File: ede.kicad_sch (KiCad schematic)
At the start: 111 parts, among them J1 Conn_01x01, J10 Conn_01x01, J11 Conn_01x01, J12 Conn_01x01, J2 Conn_01x01, J3 Conn_01x01, J4 Conn_01x01, J5 Conn_01x06, J6 Conn_01x01, J7 Conn_01x04, J8 Conn_01x04, J9 Conn_01x01, Q1 MDP10N027, Q2 MDP10N027, Q3 MDP10N027, Q4 MDP10N027, Q5 MDP10N027, Q6 MDP10N027, U1 Blackpill, U2 NCS20034DR2G, U3 STH0548S12, U4 MP1584EN_4pin, U5 U3216, U6 U3216, U7 U3216

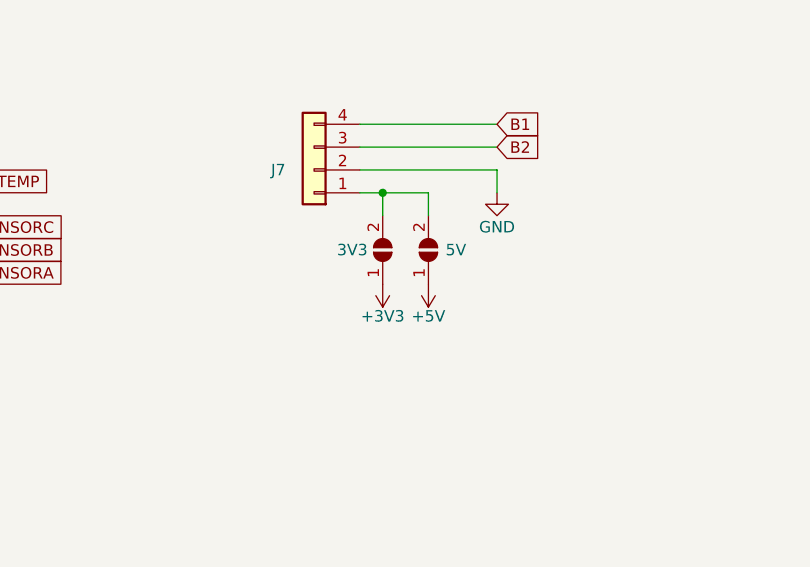
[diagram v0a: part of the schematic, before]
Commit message: sch: update JP1/2 from library, mutatis mutandis - fix ERC
Signed-off-by: Afzal <afzal@intible.in>
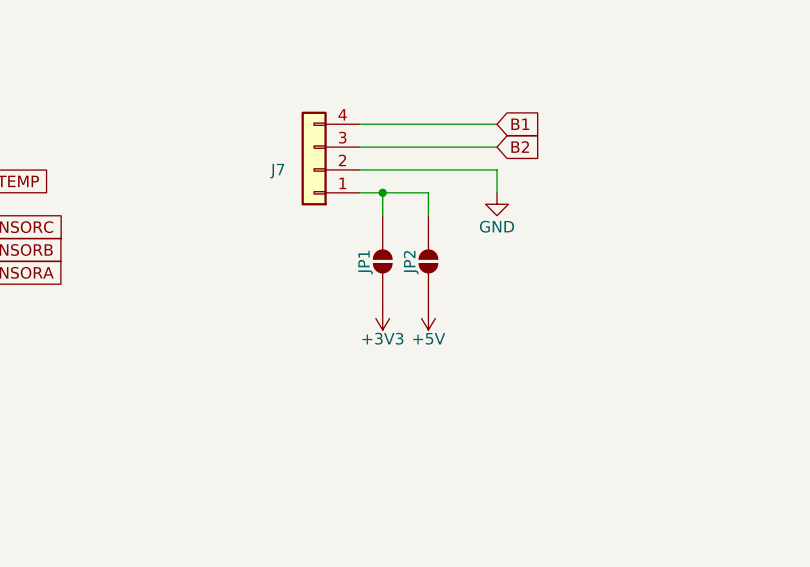
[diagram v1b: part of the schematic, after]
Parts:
- JP1: Display 3V3 -> (none); now left out of the parts list
- JP2: Display 5V -> (none); now left out of the parts list
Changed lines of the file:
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@@
 	)
 	(symbol
+		(lib_name "SolderJumper_2_Open_1")
 		(lib_id "Jumper:SolderJumper_2_Open")
-		(at 149.86 208.28 90)
+		(at 149.86 209.55 90)
 		(unit 1)
 		(body_style 1)
 		(exclude_from_sim no)
-		(in_bom yes)
+		(in_bom no)
 		(on_board yes)
 		(in_pos_files yes)
 		(dnp no)
 		(property "Reference" "JP1"
-			(at 144.78 208.28 90)
-			(hide yes)
+			(at 147.828 209.55 0)
 			(show_name no)
 			(do_not_autoplace no)
@@
 					(size 1.27 1.27)
 				)
-				(justify right)
 			)
 		)
 		(property "Value" "SolderJumper_2_Open"
-			(at 152.4 209.5499 90)
+			(at 152.4 209.55 0)
 			(hide yes)
 			(show_name no)
@@
 					(size 1.27 1.27)
 				)
-				(justify right)
 			)
 		)
 		(property "Footprint" "Intible:SolderJumper-2_small_EDE"
-			(at 149.86 208.28 0)
+			(at 149.86 209.55 0)
 			(hide yes)
 			(show_name no)
@@
 		)
 		(property "Datasheet" ""
-			(at 149.86 208.28 0)
+			(at 157.48 209.55 0)
 			(hide yes)
 			(show_name no)
@@
 			)
 		)
-		(property "Description" ""
-			(at 149.86 208.28 0)
-			(show_name no)
-			(do_not_autoplace no)
-			(effects
-				(font
-					(size 1.27 1.27)
-				)
-			)
-		)
-		(property "Display" "3V3"
-			(at 144.78 208.28 90)
+		(property "Description" "Solder Jumper, 2-pole, open"
+			(at 154.94 209.55 0)
+			(hide yes)
 			(show_name no)
 			(do_not_autoplace no)
@@
 					(size 1.27 1.27)
 				)
-				(justify right)
 			)
 		)
@@
 	(symbol
 		(lib_id "power:+5V")
-		(at 154.94 212.09 180)
+		(at 154.94 214.63 180)
 		(unit 1)
 		(body_style 1)
@@
 		(dnp no)
 		(property "Reference" "#PWR32"
-			(at 154.94 208.28 0)
+			(at 154.94 210.82 0)
 			(hide yes)
 			(show_name no)
@@
 		)
 		(property "Value" "+5V"
-			(at 154.94 215.646 0)
+			(at 154.94 218.186 0)
 			(show_name no)
 			(do_not_autoplace no)
@@
 		)
 		(property "Footprint" ""
-			(at 154.94 212.09 0)
+			(at 154.94 214.63 0)
 			(hide yes)
 			(show_name no)
@@
 		)
 		(property "Datasheet" ""
-			(at 154.94 212.09 0)
+			(at 154.94 214.63 0)
 			(hide yes)
 			(show_name no)
@@
 		)
 		(property "Description" "Power symbol creates a global label with name \"+5V\""
-			(at 154.94 212.09 0)
+			(at 154.94 214.63 0)
 			(hide yes)
 			(show_name no)
@@
 	(symbol
 		(lib_id "power:+3V3")
-		(at 149.86 212.09 180)
+		(at 149.86 214.63 180)
 		(unit 1)
 		(body_style 1)
@@
 		(dnp no)
 		(property "Reference" "#PWR31"
-			(at 149.86 208.28 0)
+			(at 149.86 210.82 0)
 			(hide yes)
 			(show_name no)
@@
 		)
 		(property "Value" "+3V3"
-			(at 149.86 215.646 0)
+			(at 149.86 218.186 0)
 			(show_name no)
 			(do_not_autoplace no)
@@
 		)
 		(property "Footprint" ""
-			(at 149.86 212.09 0)
+			(at 149.86 214.63 0)
 			(hide yes)
 			(show_name no)
@@
 		)
 		(property "Datasheet" ""
-			(at 149.86 212.09 0)
+			(at 149.86 214.63 0)
 			(hide yes)
 			(show_name no)
@@
 		)
 		(property "Description" "Power symbol creates a global label with name \"+3V3\""
-			(at 149.86 212.09 0)
+			(at 149.86 214.63 0)
 			(hide yes)
 			(show_name no)
@@
 	(symbol
 		(lib_id "Jumper:SolderJumper_2_Open")
-		(at 154.94 208.28 90)
+		(at 154.94 209.55 90)
 		(unit 1)
 		(body_style 1)
 		(exclude_from_sim no)
-		(in_bom yes)
+		(in_bom no)
 		(on_board yes)
 		(in_pos_files yes)
 		(dnp no)
 		(property "Reference" "JP2"
-			(at 156.845 208.28 90)
-			(hide yes)
+			(at 152.908 209.55 0)
 			(show_name no)
 			(do_not_autoplace no)
@@
 					(size 1.27 1.27)
 				)
-				(justify right)
 			)
 		)
 		(property "Value" "SolderJumper_2_Open"
-			(at 157.48 209.5499 90)
+			(at 157.48 209.55 0)
 			(hide yes)
 			(show_name no)
@@
 					(size 1.27 1.27)
 				)
-				(justify right)
 			)
 		)
 		(property "Footprint" "Intible:SolderJumper-2_small_EDE"
-			(at 154.94 208.28 0)
+			(at 154.94 209.55 0)
 			(hide yes)
 			(show_name no)
@@
 		)
 		(property "Datasheet" ""
-			(at 154.94 208.28 0)
+			(at 162.56 209.55 0)
 			(hide yes)
 			(show_name no)
@@
 			)
 		)
-		(property "Description" ""
-			(at 154.94 208.28 0)
-			(show_name no)
-			(do_not_autoplace no)
-			(effects
-				(font
-					(size 1.27 1.27)
-				)
-			)
-		)
-		(property "Display" "5V"
-			(at 156.845 208.28 90)
+		(property "Description" "Solder Jumper, 2-pole, open"
+			(at 160.02 209.55 0)
+			(hide yes)
 			(show_name no)
 			(do_not_autoplace no)
@@
 					(size 1.27 1.27)
 				)
-				(justify right)
 			)
 		)
